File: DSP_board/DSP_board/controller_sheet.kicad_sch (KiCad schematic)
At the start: 30 parts, among them IC1 SN74S1053NSR, IC5 F280025CPNQR, J1 Conn_01x02, J2 Conn_01x02, J3 Conn_01x02, J4 Conn_01x02, J5 1-84981-0, J6 Conn_01x02

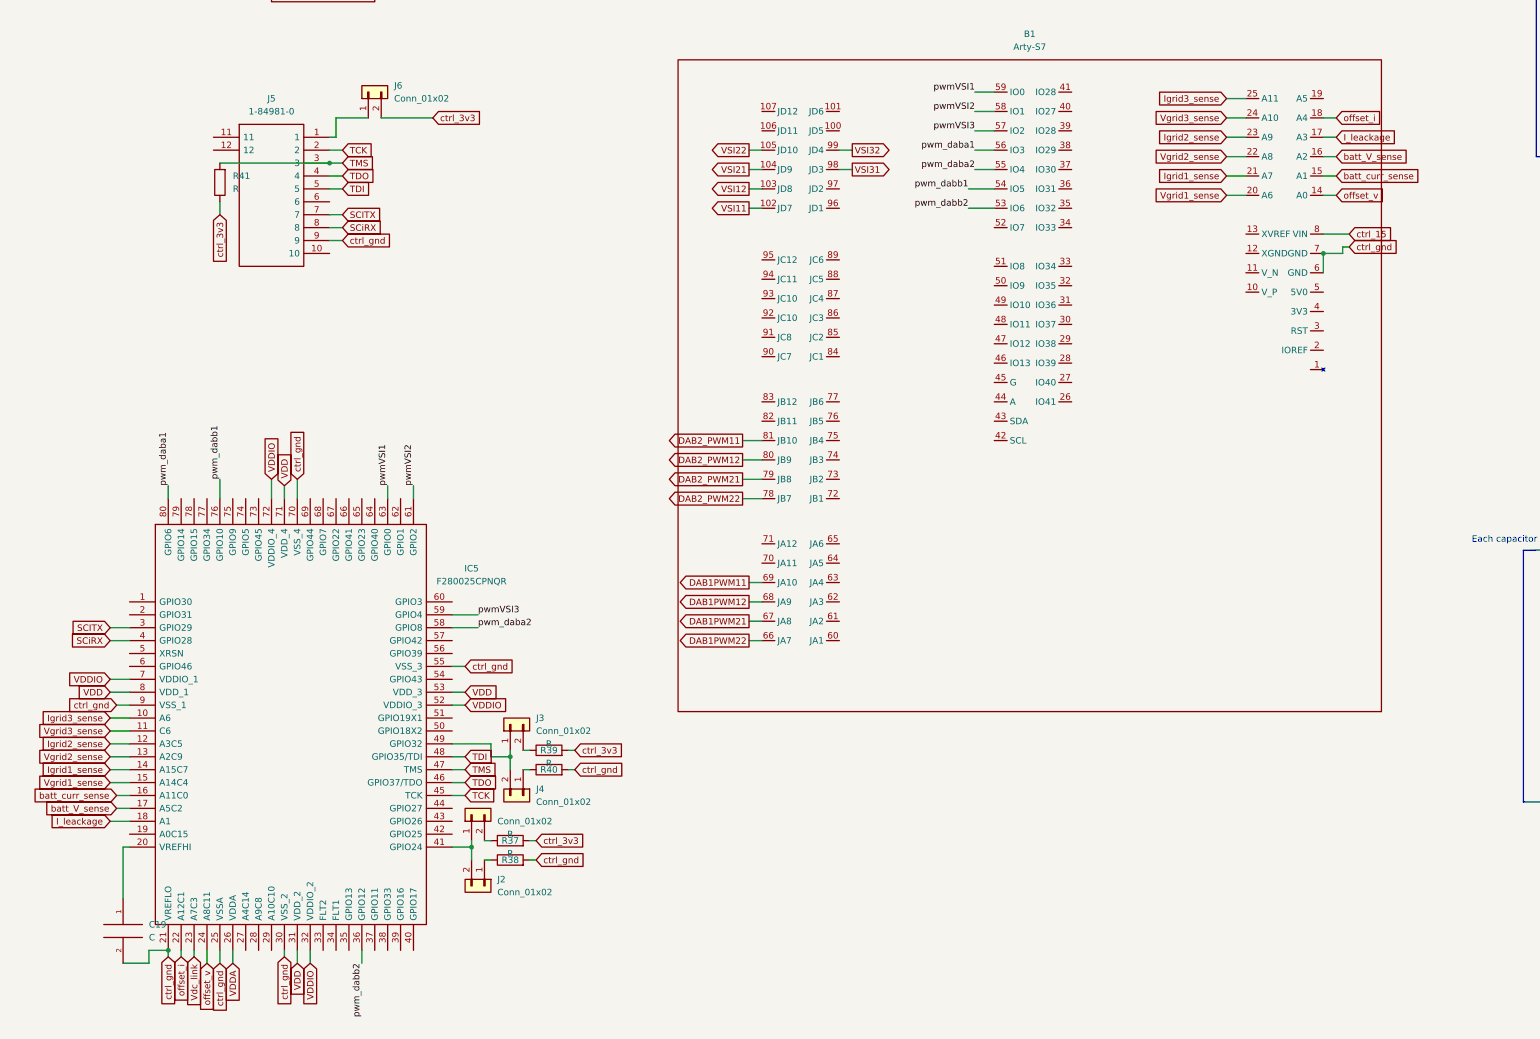
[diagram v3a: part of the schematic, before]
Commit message: adding offset measurements
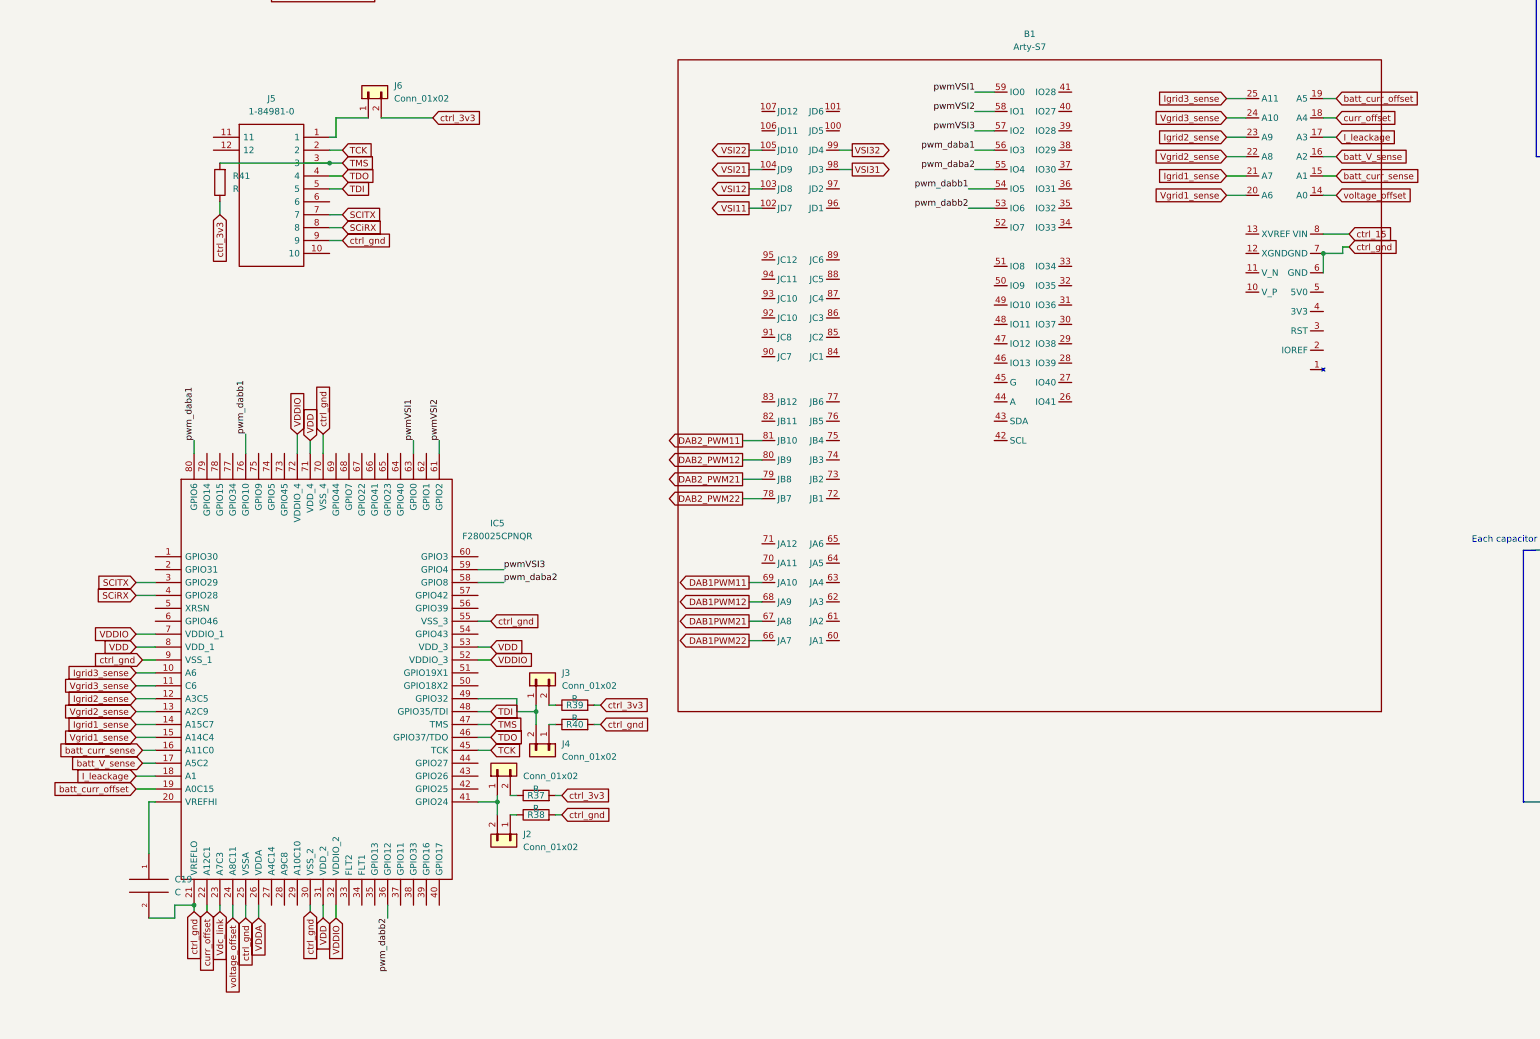
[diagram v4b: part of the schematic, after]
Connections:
- net batt_curr_offset: now reaches IC5.19 (A0C15)
- net batt_curr_offset: now also B1.19 (A5)
- net offset_i renamed curr_offset
- net offset_v renamed voltage_offset
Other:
- moved on the sheet: C19, IC5, J2, J3, J4, R37, R38, R39, R40

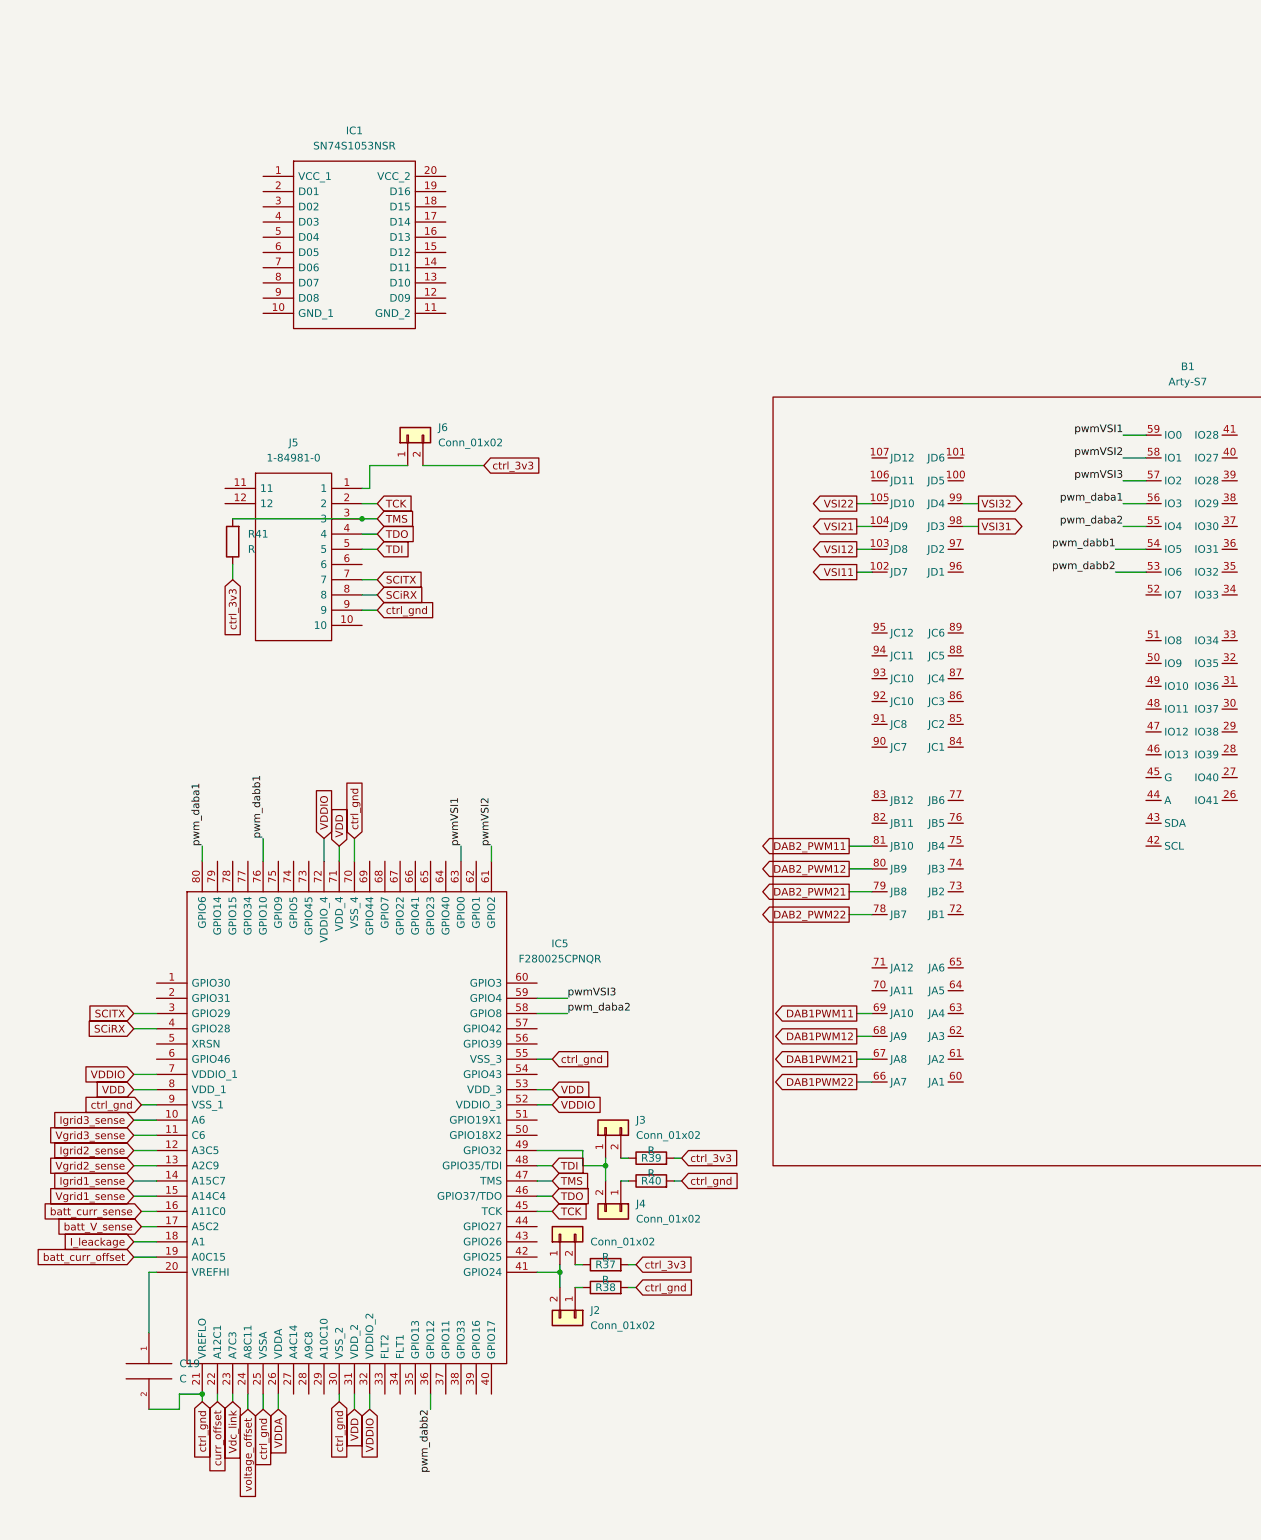
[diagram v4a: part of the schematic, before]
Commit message: connected ADC's
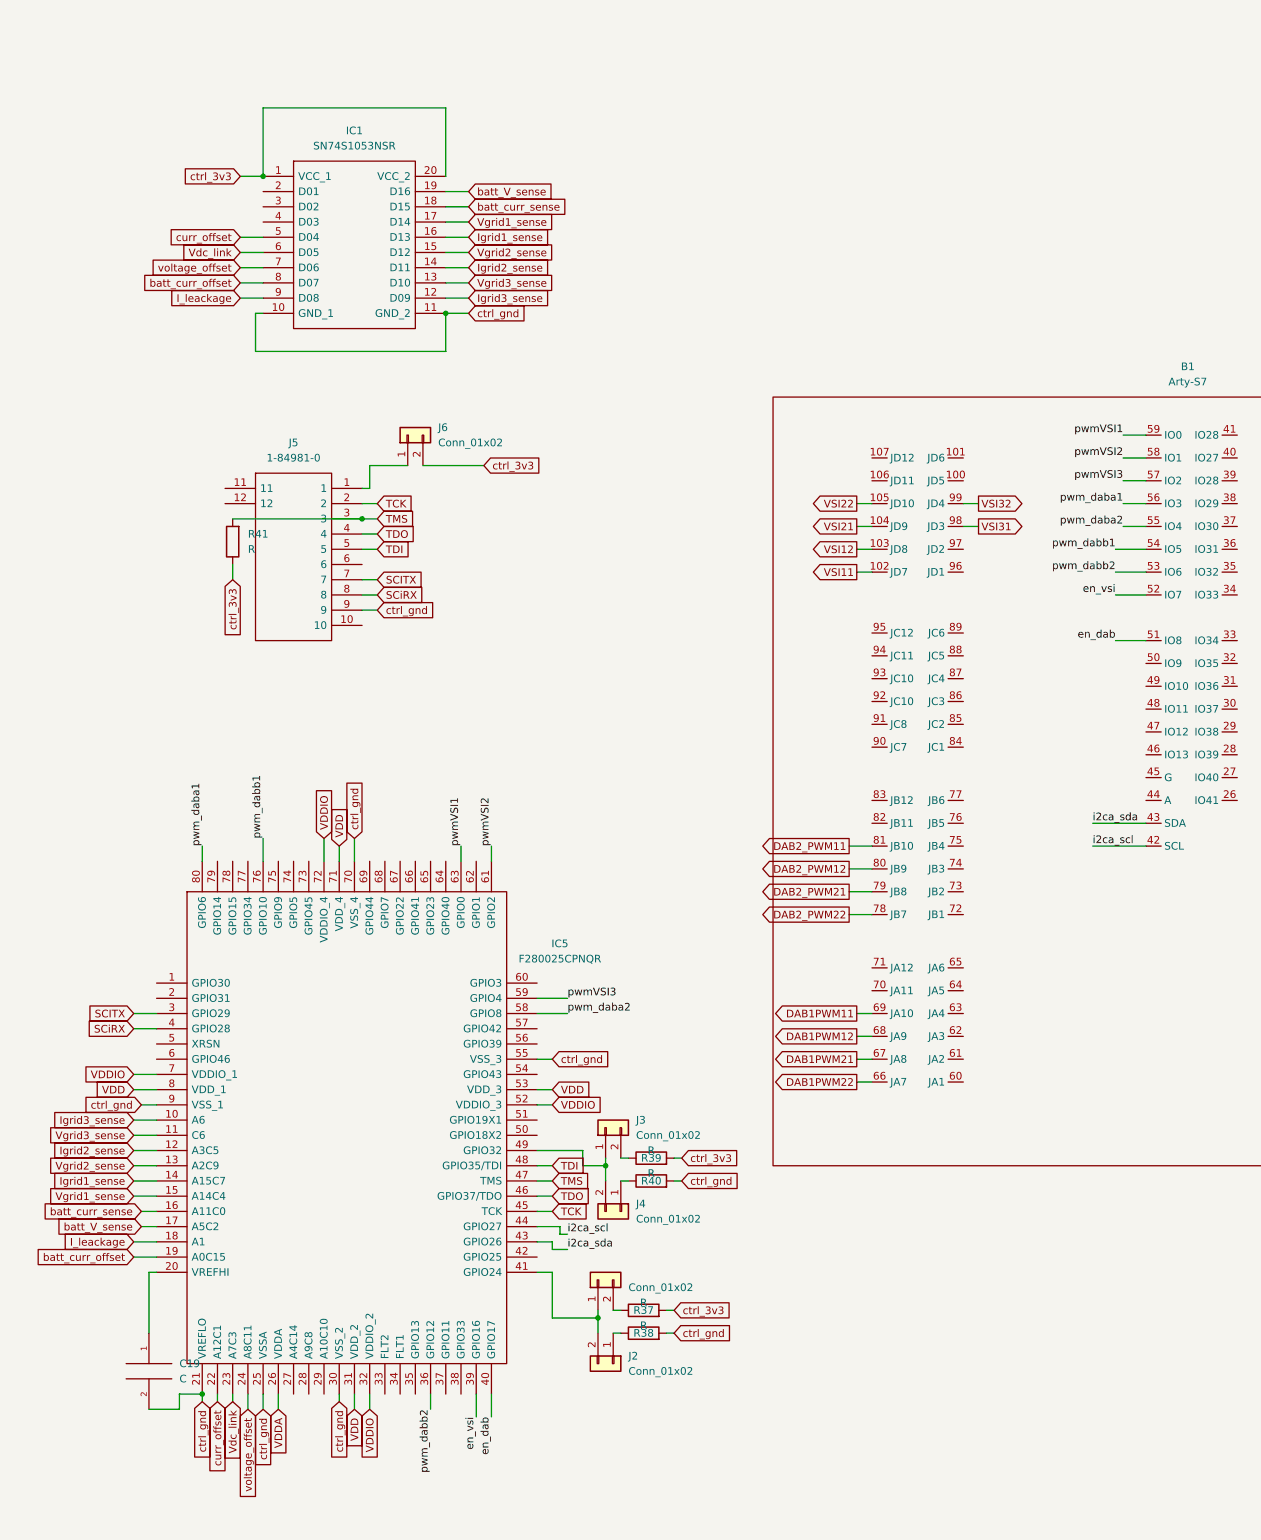
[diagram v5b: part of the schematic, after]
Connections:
- net I_leackage: now also IC1.9 (D08)
- net Igrid1_sense: now also IC1.16 (D13)
- net Igrid2_sense: now also IC1.14 (D11)
- net Igrid3_sense: now also IC1.12 (D09)
- net Vdc_link: now also IC1.6 (D05)
- net Vgrid1_sense: now also IC1.17 (D14)
- net Vgrid2_sense: now also IC1.15 (D12)
- net Vgrid3_sense: now also IC1.13 (D10)
- net batt_V_sense: now also IC1.19 (D16)
- net batt_curr_offset: now also IC1.8 (D07)
- net batt_curr_sense: now also IC1.18 (D15)
- net ctrl_3v3: now also IC1.1 (VCC_1), IC1.20 (VCC_2)
- net ctrl_gnd: now also IC1.10 (GND_1), IC1.11 (GND_2)
- net curr_offset: now also IC1.5 (D04)
- net voltage_offset: now also IC1.7 (D06)
- net en_vsi: now reaches IC5.39 (GPIO16)
- net en_vsi: now also B1.52 (IO7)
- net en_dab: now reaches IC5.40 (GPIO17)
- net en_dab: now also B1.51 (IO8)
- net i2ca_sda: now reaches IC5.43 (GPIO26)
- net i2ca_sda: now also B1.43 (SDA)
- net i2ca_scl: now reaches IC5.44 (GPIO27)
- net i2ca_scl: now also B1.42 (SCL)
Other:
- moved on the sheet: J2, R37, R38

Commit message: controller_final
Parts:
- added R10, R11, R12, R14, R17, R18, R20, R22, R24, R27, R30, R31, R34, R42, R43, R44, R45, R46, R47, R48, R49, R50, R51, R52, R9: R, Resistor_SMD:R_1206_3216Metric_Pad1.30x1.75mm_HandSolder, symbol Device:R
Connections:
- net DAB1PWM11: now also B1.63 (JA4), R49.1; no longer B1.69 (JA10)
- net DAB1PWM12: now also B1.62 (JA3), R50.1; no longer B1.68 (JA9)
- net DAB1PWM21: now also B1.61 (JA2), R51.1; no longer B1.67 (JA8)
- net DAB1PWM22: now also B1.60 (JA1), R52.1; no longer B1.66 (JA7)
- net DAB2_PWM11: now also B1.69 (JA10), R45.1; no longer B1.81 (JB10)
- net DAB2_PWM12: now also B1.68 (JA9), R46.1; no longer B1.80 (JB9)
- net DAB2_PWM21: now also B1.67 (JA8), R47.1; no longer B1.79 (JB8)
- net DAB2_PWM22: now also B1.66 (JA7), R48.1; no longer B1.78 (JB7)
- net I_leackage: now also IC1.17 (D14), IC5.15 (A14C4); no longer B1.17 (A3), IC1.9 (D08), IC5.18 (A1)
- net Igrid1_sense: no longer B1.21 (A7)
- net Igrid2_sense: now also IC1.12 (D09), IC5.10 (A6); no longer B1.23 (A9), IC1.14 (D11), IC5.12 (A3C5)
- net Igrid3_sense: now also IC1.13 (D10), IC5.11 (C6); no longer B1.25 (A11), IC1.12 (D09), IC5.10 (A6)
- net VSI11: now also R44.1
- net VSI12: now also B1.96 (JD1), R34.1; no longer B1.103 (JD8)
- net VSI21: now also B1.103 (JD8), R43.1; no longer B1.104 (JD9)
- net VSI22: now also B1.97 (JD2), R31.1; no longer B1.105 (JD10)
- net VSI31: now also B1.104 (JD9), R42.1; no longer B1.98 (JD3)
- net VSI32: now also B1.98 (JD3), R30.1; no longer B1.99 (JD4)
- net Vdc_link: now also IC1.4 (D03), IC5.17 (A5C2); no longer IC1.6 (D05), IC5.23 (A7C3)
- net Vgrid1_sense: now also IC1.18 (D15), IC5.16 (A11C0); no longer B1.20 (A6), IC1.17 (D14), IC5.15 (A14C4)
- net Vgrid2_sense: no longer B1.22 (A8)
- net Vgrid3_sense: now also IC1.14 (D11), IC5.12 (A3C5); no longer B1.24 (A10), IC1.13 (D10), IC5.11 (C6)
- net batt_V_sense: now also IC1.2 (D01), IC5.19 (A0C15); no longer B1.16 (A2), IC1.19 (D16), IC5.17 (A5C2)
- net batt_curr_sense: now also IC1.3 (D02), IC5.18 (A1); no longer B1.15 (A1), IC1.18 (D15), IC5.16 (A11C0)
- net ctrl_gnd: now also R11.2, R12.2, R14.2, R17.2, R18.2, R20.2, R22.2, R24.2, R27.2, R30.2, R31.2, R34.2, R42.2, R43.2, R44.2, R45.2, R46.2, R47.2, R48.2, R49.2, R50.2, R51.2, R52.2
- net en_dab: now also IC5.56 (GPIO39), R27.1; no longer IC5.40 (GPIO17)
- net en_vsi: now also IC5.57 (GPIO42), R24.1; no longer IC5.39 (GPIO16)
- net pwmVSI1: now also B1.57 (IO2), R14.1; no longer B1.59 (IO0)
- net pwmVSI2: now also B1.56 (IO3), R17.1; no longer B1.58 (IO1)
- net pwmVSI3: now also B1.55 (IO4), R18.1; no longer B1.57 (IO2)
- net pwm_daba1: now also B1.59 (IO0), R11.1; no longer B1.56 (IO3)
- net pwm_daba2: now also B1.54 (IO5), R20.1; no longer B1.55 (IO4)
- net pwm_dabb1: now also B1.58 (IO1), R12.1; no longer B1.54 (IO5)
- net pwm_dabb2: now also R22.1
- net dc_ready: now reaches IC5.35 (GPIO13)
- net dc_fault: now reaches IC5.37 (GPIO11)
- net OCD_leakage: now reaches IC5.38 (GPIO33)
- net vsi_ready: now reaches IC5.74 (GPIO5)
- net vsi_ready: now also B1.93 (JC10)
- net vsi_fault: now reaches IC5.75 (GPIO9)
- net vsi_fault: now also B1.92 (JC10)
- net OCD_grid3: now reaches IC5.77 (GPIO34)
- net OCD_grid3: now also B1.91 (JC8)
- net OCD_grd2: now reaches IC5.78 (GPIO15)
- net OCD_grd2: now also B1.90 (JC7)
- net OCD_grid1: now reaches IC5.79 (GPIO14)
- net OCD_grid1: now also B1.84 (JC1)
- net FPGA_3v3: now reaches B1.4 (3V3)
- net FPGA_3v3: now also R10.2, R9.2
- removed net batt_curr_offset: B1.19 (A5), IC1.8 (D07), IC5.19 (A0C15)
- removed net curr_offset: B1.18 (A4), IC1.5 (D04), IC5.22 (A12C1)
- net i2ca_scl renamed SCL
- net SCL: now also R10.1
- net i2ca_sda renamed SDA
- net SDA: now also R9.1
- removed net voltage_offset: B1.14 (A0), IC1.7 (D06), IC5.24 (A8C11)
- new net batt_fault: IC5.39 (GPIO16)
- new net batt_ready: IC5.40 (GPIO17)
- new net offset_v: IC1.8 (D07), IC5.22 (A12C1)
